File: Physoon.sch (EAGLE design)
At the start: 36 parts, among them IC2 74AHC1G125DBV, IC3 74AHC1G125DBV, M1 HX1, X1 BU-SMA-V

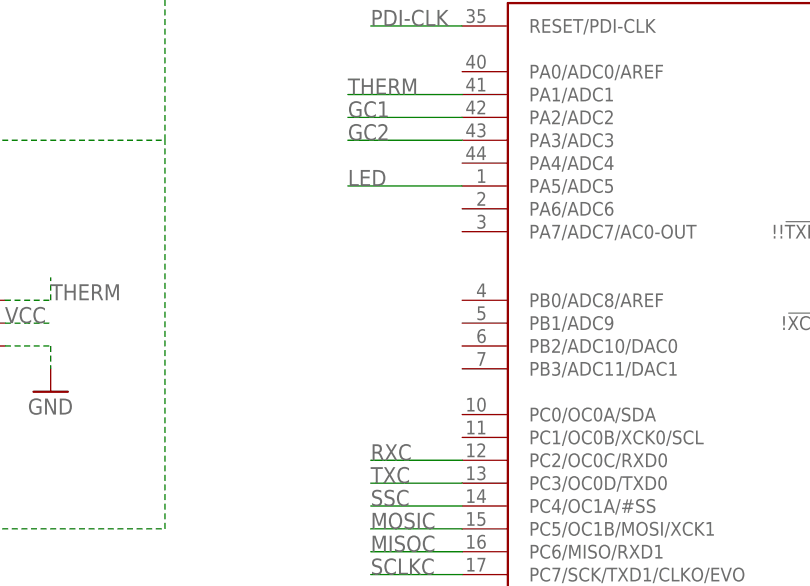
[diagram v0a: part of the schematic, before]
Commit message: Move LED to "the right" port
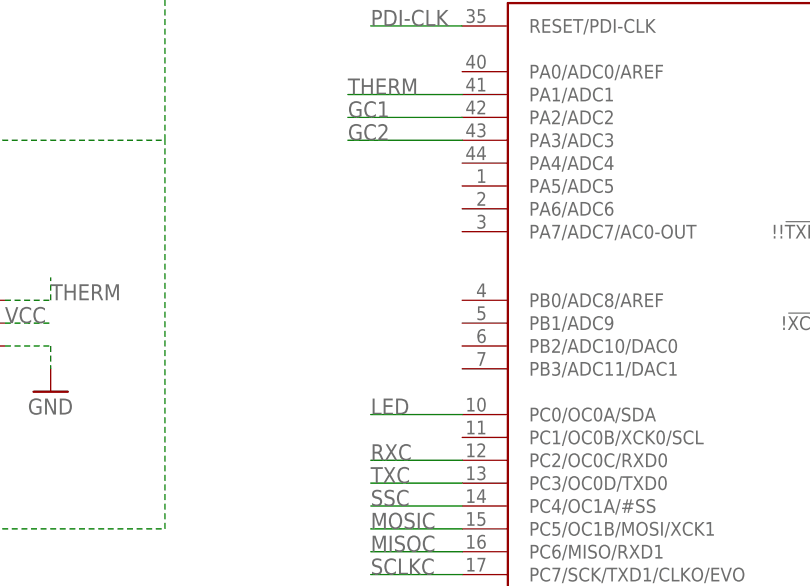
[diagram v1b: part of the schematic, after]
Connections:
- net LED: now also IC1.PC0/OC0A/SDA; no longer IC1.PA5/ADC5
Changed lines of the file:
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@@
 <?xml version="1.0" encoding="utf-8"?>
 <!DOCTYPE eagle SYSTEM "eagle.dtd">
-<eagle version="6.5.0">
+<eagle version="7.6.0">
 <drawing>
 <settings>
@@
 </segment>
 <segment>
-<pinref part="IC1" gate="G$1" pin="PA5/ADC5"/>
-<wire x1="48.26" y1="88.9" x2="35.56" y2="88.9" width="0.1524" layer="91"/>
-<label x="35.56" y="88.9" size="1.778" layer="95"/>
-</segment>
-</net>
+<pinref part="IC1" gate="G$1" pin="PC0/OC0A/SDA"/>
+<wire x1="48.26" y1="63.5" x2="38.1" y2="63.5" width="0.1524" layer="91"/>
+<label x="38.1" y="63.5" size="1.778" layer="95"/>
+</segment>
+</net>
